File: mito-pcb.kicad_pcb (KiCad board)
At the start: 4 copper layers, 228 x 84.3 mm, 107 parts, among them SW10 SW_Push, SW11 SW_Push, SW12 SW_Push, SW13 SW_Push, SW14 SW_Push, SW15 SW_Push, SW16 SW_Push, SW17 SW_Push, SW18 SW_Push, SW19 SW_Push, SW20 SW_Push, SW21 SW_Push, SW22 SW_Push, SW23 SW_Push, SW26 SW_Push, SW27 SW_Push, SW28 SW_Push, SW29 SW_Push, SW3 SW_Push, SW30 SW_Push, SW31 SW_Push, SW32 SW_Push, SW33 SW_Push, SW34 SW_Push, SW35 SW_Push, SW36 SW_Push, SW37 SW_Push, SW38 SW_Push, SW39 SW_Push, SW4 SW_Push, SW40 SW_Push, SW41 SW_Push, SW42 SW_Push, SW43 SW_Push, SW44 SW_Push, SW45 SW_Push, SW46 SW_Push, SW5 SW_Push, SW6 SW_Push, SW7 SW_Push, SW8 SW_Push, SW9 SW_Push, U1 XIAO-nRF52840-SMD, U3 XIAO-nRF52840-SMD

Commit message: changed xioa footprint, edited edge cuts, layed out
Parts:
- TP1, TP2: moved to B.Cu
- moved TP1 246.0 mm to (234.6, 80.2), turned to 180 degrees
- moved TP2 90.0 mm to (56.1, 79.2), turned to 180 degrees
- moved TP8 53.8 mm to (56.8, 84.2)
- moved R2 33.1 mm to (238.5, 83.9), turned to 0 degrees
- moved R3 30.3 mm to (238.5, 86.4), turned to 180 degrees
- moved R9 29.2 mm to (53.3, 82.2), turned to 180 degrees
- moved R10 26.8 mm to (53.3, 84.2), turned to 0 degrees
- moved U1 1.85 mm to (248.7, 99.0)
- moved U3 0.61 mm to (40.8, 99.0)
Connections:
- U1 pad 10: unconnected-(U1-P1.14_D9_MISO-Pad10) -> /left/ROW1
- U1 pad 11: unconnected-(U1-P1.15_D10_MOSI-Pad11) -> /left/ROW0
- U1 pad 2: unconnected-(U1-P0.03_A1_D1-Pad2) -> /left/COL0
- U1 pad 3: unconnected-(U1-P0.28_A2_D2-Pad3) -> /left/COL1
- U1 pad 4: unconnected-(U1-P0.29_A3_D3-Pad4) -> /left/COL2
- U1 pad 5: unconnected-(U1-P0.04_A4_D4_SDA-Pad5) -> /left/COL3
- U1 pad 6: unconnected-(U1-P0.05_A5_D5_SCL-Pad6) -> /left/COL4
- U1 pad 7: unconnected-(U1-P1.11_D6_TX-Pad7) -> /left/ROW4
- U1 pad 8: unconnected-(U1-P1.12_D7_RX-Pad8) -> /left/ROW3
- U1 pad 9: unconnected-(U1-P1.13_D8_SCK-Pad9) -> /left/ROW2
- U3 pad 10: unconnected-(U3-P1.14_D9_MISO-Pad10) -> /right/ROW1
- U3 pad 11: unconnected-(U3-P1.15_D10_MOSI-Pad11) -> /right/ROW0
- U3 pad 2: unconnected-(U3-P0.03_A1_D1-Pad2) -> /right/COL0
- U3 pad 3: unconnected-(U3-P0.28_A2_D2-Pad3) -> /right/COL1
- U3 pad 4: unconnected-(U3-P0.29_A3_D3-Pad4) -> /right/COL2
- U3 pad 5: unconnected-(U3-P0.04_A4_D4_SDA-Pad5) -> /right/COL3
- U3 pad 6: unconnected-(U3-P0.05_A5_D5_SCL-Pad6) -> /right/COL4
- U3 pad 7: unconnected-(U3-P1.11_D6_TX-Pad7) -> /right/ROW4
- U3 pad 8: unconnected-(U3-P1.12_D7_RX-Pad8) -> /right/ROW3
- U3 pad 9: unconnected-(U3-P1.13_D8_SCK-Pad9) -> /right/ROW2
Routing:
- net (no net): track 134.1 -> 0.00 mm
- net GND: track 11.7 -> 0.00 mm
- removed copper zone on In1.Cu, net (none)
- removed copper zone on In2.Cu, net GND
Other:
- outline, holes or cut-outs redrawn
- copper layers 4 -> 2

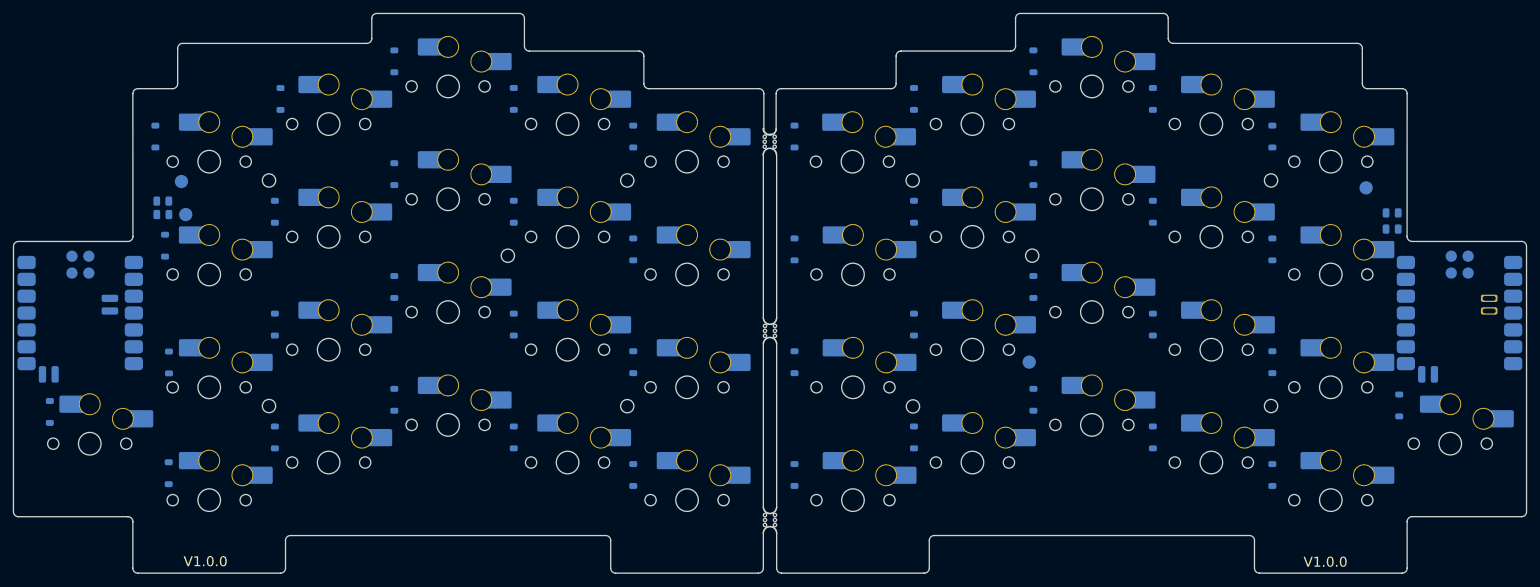
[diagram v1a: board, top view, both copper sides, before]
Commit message: routed left half
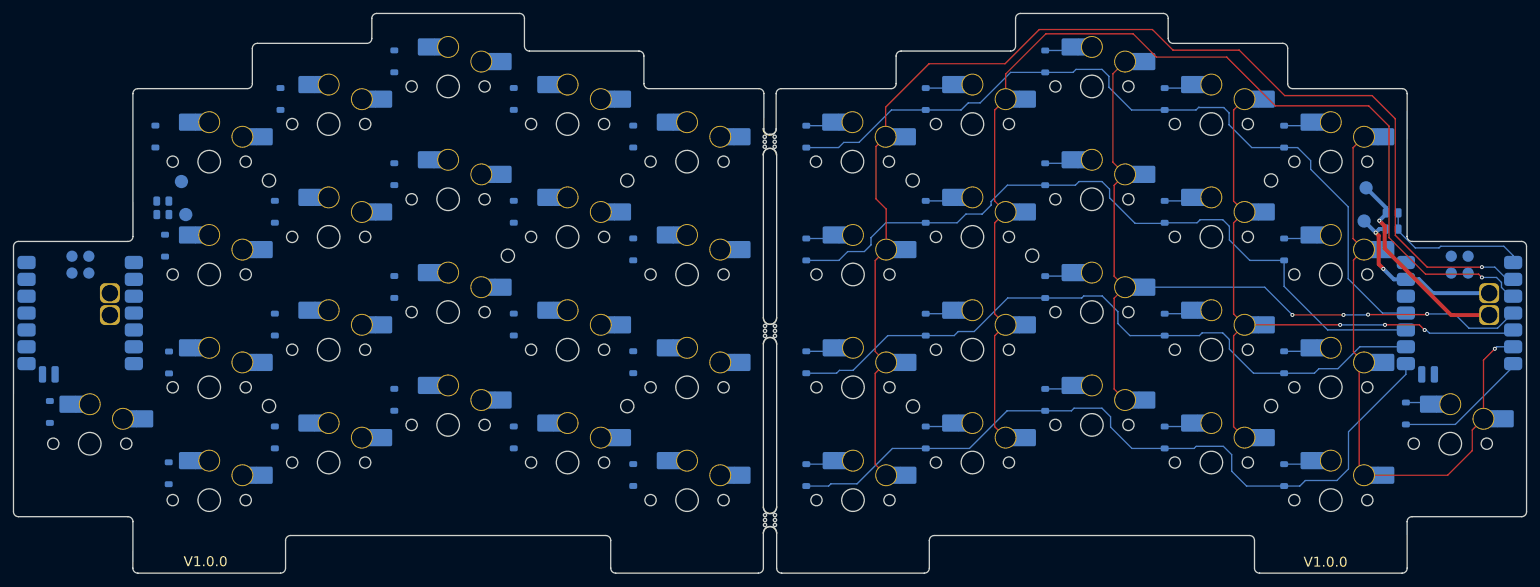
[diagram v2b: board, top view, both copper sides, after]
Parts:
- U1, U3: footprint Seeed Studio XIAO Series Library:XIAO-nRF52840-SMD -> mito-simplified:XIAO-nRF52840-SMD
- moved TP4 54.8 mm to (234.3, 85.2)
- moved D10 1.78 mm to (204.2, 83.8)
- moved D11 1.78 mm to (222.2, 89.4)
- moved D12 1.78 mm to (150.2, 106.4)
- moved D13 1.78 mm to (168.2, 100.8)
- moved D14 1.78 mm to (186.2, 95.1)
- moved D15 1.78 mm to (204.2, 100.8)
- moved D16 1.78 mm to (222.2, 106.4)
- moved D17 1.78 mm to (150.2, 123.4)
- moved D18 1.78 mm to (168.2, 117.8)
- moved D19 1.78 mm to (186.2, 112.1)
- moved D2 1.78 mm to (150.2, 72.4)
- moved D20 1.78 mm to (204.2, 117.8)
- moved D21 1.78 mm to (222.2, 123.4)
- moved D3 1.78 mm to (168.2, 66.8)
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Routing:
- net /left/COL0: track 0.00 -> 184.7 mm, vias 0 -> 1
- net /left/COL1: track 0.00 -> 164.5 mm, vias 0 -> 1
- net /left/ROW0: track 0.00 -> 119.9 mm
- net /left/ROW3: track 0.00 -> 114.6 mm
- net /left/COL2: track 0.00 -> 114.1 mm, vias 0 -> 4
- net /left/ROW1: track 0.00 -> 110.2 mm
- net /left/ROW2: track 0.00 -> 103.9 mm
- net /left/COL3: track 0.00 -> 96.3 mm, vias 0 -> 3
- net /left/COL4: track 0.00 -> 91.8 mm, vias 0 -> 1
- net /left/VBAT: track 0.00 -> 31.0 mm, vias 0 -> 1
- net GND: track 0.00 -> 27.7 mm, vias 0 -> 2
- net /left/BT_PIN: track 0.00 -> 22.8 mm
- net /left/ROW4: track 0.00 -> 20.2 mm
- net Net-(D4-A): track 0.00 -> 4.01 mm
- net Net-(D9-A): track 0.00 -> 4.01 mm
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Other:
- outline, holes or cut-outs redrawn

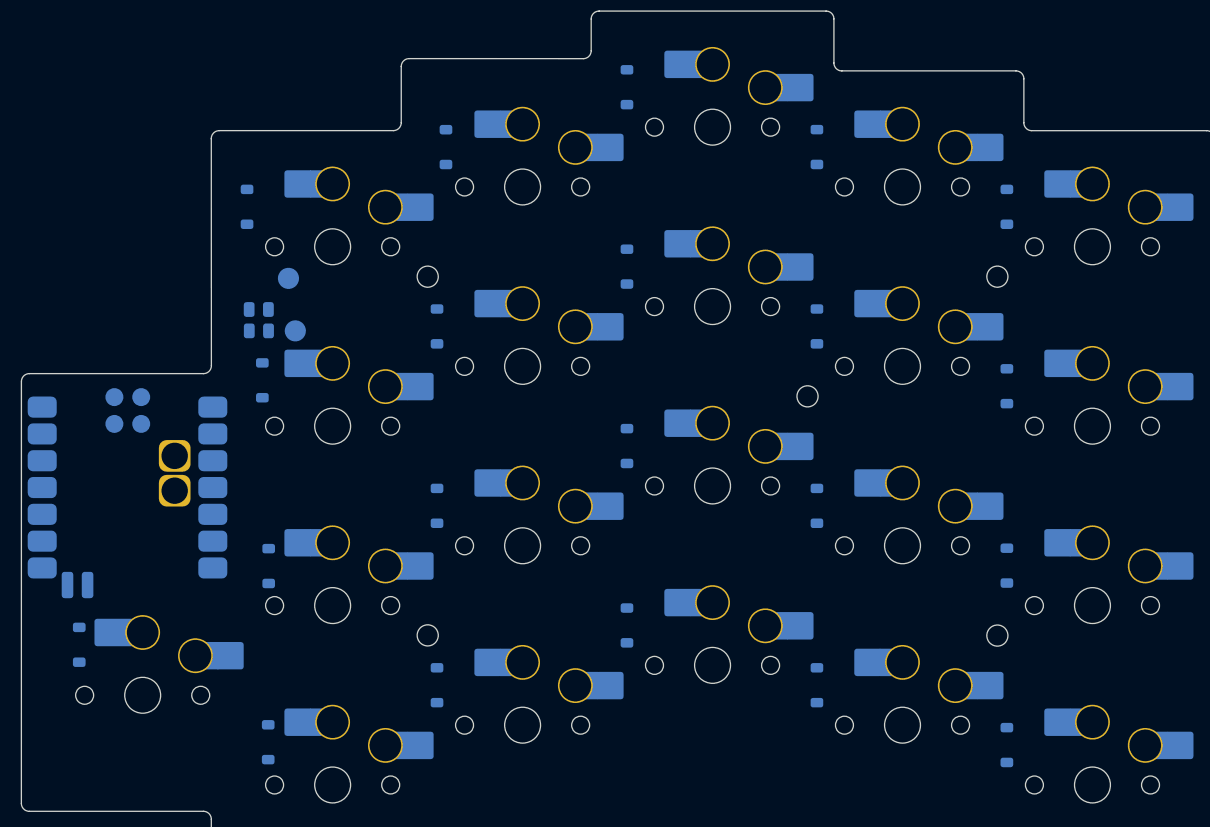
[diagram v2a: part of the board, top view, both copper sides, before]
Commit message: routed other half,added models
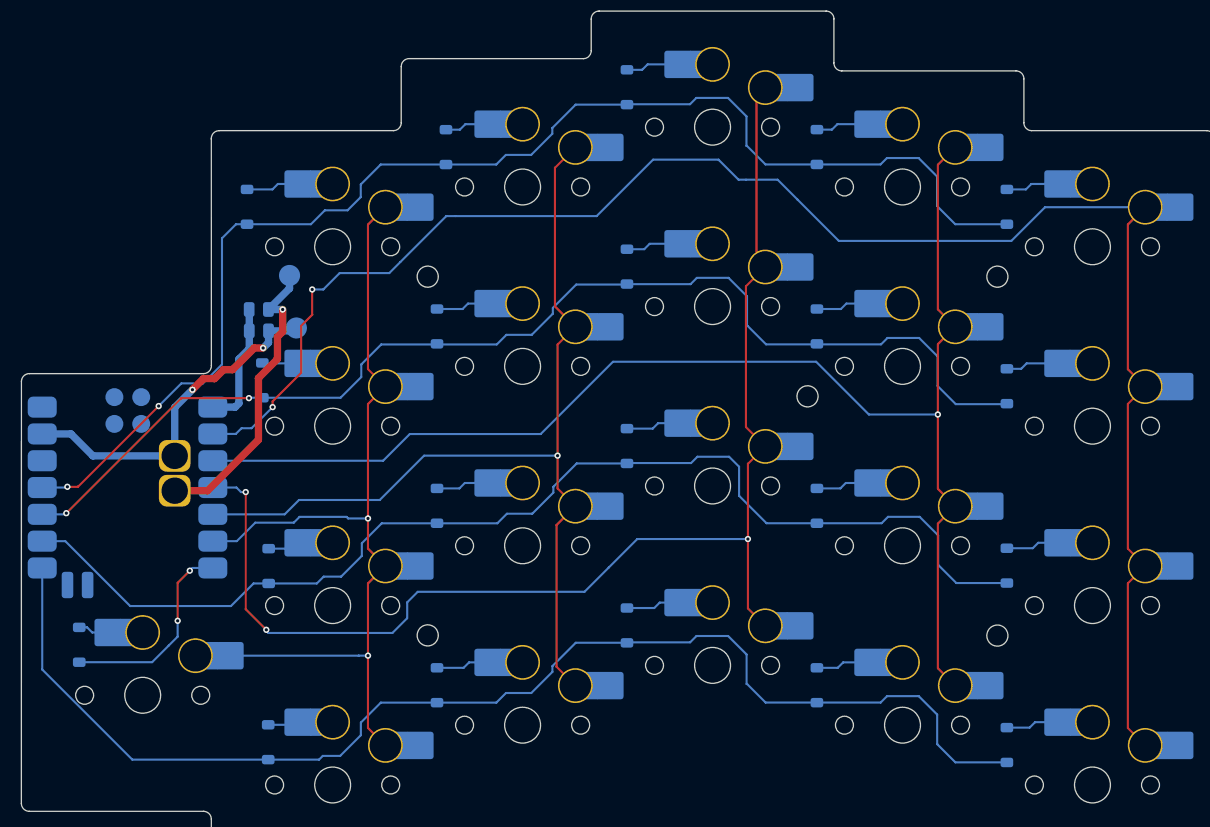
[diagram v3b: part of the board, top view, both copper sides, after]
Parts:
- moved TP2 0.29 mm to (56.2, 78.9)
- moved TP8 0.29 mm to (56.9, 83.9)
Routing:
- net /right/COL0: track 0.00 -> 163.1 mm, vias 0 -> 2
- net /right/COL1: track 0.00 -> 129.8 mm, vias 0 -> 1
- net /right/ROW0: track 0.00 -> 123.5 mm, vias 0 -> 2
- net /right/COL2: track 0.00 -> 122.2 mm, vias 0 -> 3
- net /right/ROW3: track 0.00 -> 119.2 mm
- net /right/ROW1: track 0.00 -> 110.5 mm, vias 0 -> 2
- net /right/ROW2: track 0.00 -> 109.7 mm
- net /right/COL3: track 0.00 -> 90.4 mm, vias 0 -> 1
- net /right/COL4: track 0.00 -> 83.9 mm, vias 0 -> 2
- net GND: track 27.7 -> 61.0 mm, vias 2 -> 4
- net /right/VBAT: track 0.00 -> 28.6 mm, vias 0 -> 1
- net /right/ROW4: track 0.00 -> 19.3 mm, vias 0 -> 2
- net /right/BT_PIN: track 0.00 -> 11.9 mm
- net Net-(D62-A): track 0.00 -> 5.08 mm
- net Net-(D61-A): track 0.00 -> 5.08 mm
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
